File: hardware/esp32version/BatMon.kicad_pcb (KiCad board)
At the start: 2 copper layers, 47 x 24.1 mm, 30 parts, among them J1 Battery Connector, J2 Battery_Passthrough, J3 Conn_01x06_Pin, J4 RESET, Q1 Q_PMOS_DDGSDD_TSOP-6, Q2 Q_PMOS_DDGSDD_TSOP-6, Q3 SS8050-G, U1 ESP32-WROOM-32D, U2 LM2904, U3 AMS1117

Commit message: updated PCB
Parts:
- added R10: 22k, Resistor_SMD:R_0603_1608Metric_Pad0.98x0.95mm_HandSolder, F.Cu at (161.6, 54.6)
- added R3: 5k, Resistor_SMD:R_0603_1608Metric_Pad0.98x0.95mm_HandSolder, F.Cu at (161.6, 49.6)
- added R9: 22k, Resistor_SMD:R_0603_1608Metric_Pad0.98x0.95mm_HandSolder, F.Cu at (161.6, 52.1)
- D1, D2: value D_Zener -> D_Zener_ANK
- J1: value Battery Connector -> Battery_Connector
- J2: value Battery_Passthrough -> Charging_Connector
- J3: value Conn_01x06_Pin -> Prog_Connector
- R11: value k -> 22k
- U2: footprint Package_DIP:DIP-8_W8.89mm_SMDSocket_LongPads -> Package_SO:SOIC-8_3.9x4.9mm_P1.27mm
- moved D1 35.4 mm to (156.0, 50.6)
- moved D2 33.0 mm to (155.4, 58.1)
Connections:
- net Cell2 renamed C2ADC
- net Net-(J1-Pin_2) renamed /C1RAW
- net Net-(J1-Pin_3) renamed /C2RAW
- C1 pad 2: GND -> CGND
- C2 pad 1: +BATT -> C2IN
- C2 pad 2: GND -> CGND
- C3 pad 2: GND -> CGND
- C4 pad 2: GND -> CGND
- C5 pad 2: GND -> CGND
- D1 pad 1: +BATT -> Net-(Q1-G)
- D1 pad 2: Net-(D1-A) -> unconnected-(D1-A-Pad2)
- D1 pad 3: (no net) -> C2IN
- D2 pad 1: C1IN -> Net-(Q2-G)
- D2 pad 2: Net-(D2-A) -> unconnected-(D2-A-Pad2)
- D2 pad 3: (no net) -> C1IN
- J1 pad 1: GND -> CGND
- J2 pad 5: GND -> CGND
- J3 pad 5: GND -> CGND
- J4 pad 1: GND -> CGND
- Q1 pad 3: Net-(D1-A) -> Net-(Q1-G)
- Q1 pad 4: +BATT -> C2IN
- Q2 pad 3: Net-(D2-A) -> Net-(Q2-G)
- Q3 pad 2: GND -> CGND
- R11 pad 2: +BATT -> C2IN
- R12 pad 1: GND -> CGND
- R4 pad 1: GND -> Net-(U2A--)
- R4 pad 2: Net-(U2A--) -> CGND
- R6 pad 2: GND -> CGND
- R7 pad 2: Net-(D1-A) -> Net-(Q1-G)
- R8 pad 1: GND -> CGND
- R8 pad 2: Net-(D2-A) -> Net-(Q2-G)
- U1 pad 1: GND -> CGND
- U1 pad 15: GND -> CGND
- U1 pad 27: Cell1 -> C1ADC
- U1 pad 38: GND -> CGND
- U1 pad 39: GND -> CGND
- U2 pad 4: GND -> CGND
- U3 pad 1: GND -> CGND
- U3 pad 3: +BATT -> C2IN
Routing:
- net C2IN: track 0.00 -> 28.0 mm, vias 0 -> 2
- net +BATT: track 28.0 -> 0.00 mm, vias 2 -> 0
- net GND: track 81.4 -> 64.1 mm, vias 5 -> 0
- net CGND: track 0.00 -> 17.3 mm, vias 0 -> 5
- net Net-(Q1-G): track 0.00 -> 12.7 mm
- net Net-(D1-A): track 12.7 -> 0.00 mm
- net Net-(Q2-G): track 0.00 -> 11.7 mm
- net Net-(D2-A): track 11.7 -> 0.00 mm
- added copper zone on B.Cu, net CGND
- added copper zone on F.Cu, net CGND
- removed copper zone on B.Cu, net GND
- removed copper zone on F.Cu, net GND

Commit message: started working on new layout
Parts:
- removed J2: Charging_Connector, Connector_PinHeader_2.54mm:PinHeader_1x05_P2.54mm_Horizontal
- removed J4: RESET, Connector_PinHeader_2.54mm:PinHeader_1x02_P2.54mm_Vertical
- removed the R10 at (135.7, 81.3)
- removed the R10 at (161.6, 54.6)
- removed the R3 at (161.6, 49.6)
- removed the R3 at (115.8, 80.2)
- removed the R9 at (118.3, 79.2)
- removed the R9 at (161.6, 52.1)
- removed U3: AMS1117, Package_TO_SOT_SMD:SOT-223-3_TabPin2
- added D3: D_Schottky, Diode_SMD:D_SOD-123, F.Cu at (101.2, 68.6)
- added D4: LED, LED_SMD:LED_0603_1608Metric_Pad1.05x0.95mm_HandSolder, F.Cu at (108.0, 67.3)
- added D5: ~, ELEKTRON_Footprints:D_TVS_Quad_Array_1206, B.Cu at (142.6, 81.3)
- added J5: Charging_Connector, ELEKTRON_Footprints:Conn_Edge_1x6_LLSSSS_Mirrored, F.Cu at (149.0, 79.0)
- added R10: 22k, Resistor_SMD:R_0603_1608Metric_Pad0.98x0.95mm_HandSolder, F.Cu at (162.6, 63.5)
- added R3: R, Resistor_SMD:R_0603_1608Metric_Pad0.98x0.95mm_HandSolder, F.Cu at (114.7, 68.6)
- added R9: 20k, Resistor_SMD:R_0603_1608Metric_Pad0.98x0.95mm_HandSolder, F.Cu at (228.8, 110.5)
- added U4: AZ1117CR-3.3, Package_TO_SOT_SMD:SOT-89-3_Handsoldering, F.Cu at (196.0, 64.8)
- BZ1, U1: moved to F.Cu
- C1: footprint Capacitor_SMD:C_0603_1608Metric_Pad1.08x0.95mm_HandSolder -> Capacitor_Tantalum_SMD:CP_EIA-3216-18_Kemet-A_Pad1.58x1.35mm_HandSolder
- C2: value 100n -> 22µ; footprint Capacitor_SMD:C_0603_1608Metric_Pad1.08x0.95mm_HandSolder -> Capacitor_Tantalum_SMD:CP_EIA-3216-18_Kemet-A_Pad1.58x1.35mm_HandSolder
- J1: footprint Connector_PinHeader_2.54mm:PinHeader_1x03_P2.54mm_Horizontal -> Connector_JST:JST_XH_S3B-XH-A_1x03_P2.50mm_Horizontal
- J3: footprint Connector_PinHeader_2.54mm:PinHeader_1x06_P2.54mm_Vertical -> ELEKTRON_Footprints:Dbg_Port_1x6_P1.27mm_ThroughHole
- R1: value 5k -> 30k
- R11: value 22k -> 30k
- R2, R4: value 5k -> 10k
- moved R6 122.5 mm to (224.5, 115.5), turned to 0 degrees
- moved R5 120.1 mm to (224.5, 113.0), turned to 0 degrees
- moved R4 114.3 mm to (224.5, 110.5), turned to 0 degrees
- moved R8 106.5 mm to (228.8, 108.0), turned to 0 degrees
- moved C4 102.4 mm to (204.5, 74.9)
- moved R11 101.6 mm to (214.6, 61.0), turned to 0 degrees
- moved R2 101.4 mm to (207.4, 61.0)
- moved R12 96.6 mm to (209.2, 58.4), turned to 0 degrees
- moved R1 92.7 mm to (203.2, 57.1), turned to 0 degrees
- moved U2 91.6 mm to (195.9, 58.6), turned to 0 degrees
- moved C5 87.1 mm to (204.5, 78.7), turned to 0 degrees
- moved C1 86.0 mm to (197.0, 48.2), turned to 0 degrees
- moved C2 82.1 mm to (197.0, 51.4), turned to 0 degrees
- moved D1 69.0 mm to (97.8, 87.6)
- moved BZ1 66.3 mm to (191.3, 85.9), turned to 0 degrees
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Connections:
- net /C1RAW renamed Net-(D5D-A1)
- net /C2RAW renamed Net-(D5C-A1)
- C1 pad 2: CGND -> GND
- C2 pad 2: CGND -> GND
- C3 pad 2: CGND -> GND
- C4 pad 2: CGND -> GND
- C5 pad 2: CGND -> GND
- J1 pad 1: CGND -> GND
- J3 pad 5: CGND -> GND
- Q3 pad 2: CGND -> GND
- R1 pad 1: Net-(U2B--) -> Net-(U2B-+)
- R1 pad 2: Net-(U2A-+) -> C2IN
- R11 pad 1: Net-(U2B-+) -> Net-(U2B--)
- R11 pad 2: C2IN -> C1IN
- R12 pad 1: CGND -> C2ADC
- R12 pad 2: Net-(U2B-+) -> Net-(U2B--)
- R2 pad 1: Net-(U2A-+) -> Net-(U2B-+)
- R2 pad 2: C2ADC -> GND
- R4 pad 1: Net-(U2A--) -> C1ADC
- R4 pad 2: CGND -> GND
- R6 pad 2: CGND -> GND
- R8 pad 1: CGND -> GND
- U1 pad 1: CGND -> GND
- U1 pad 11: unconnected-(U1-IO26-Pad11) -> Net-(U1-IO26)
- U1 pad 15: CGND -> GND
- U1 pad 38: CGND -> GND
- U1 pad 39: CGND -> GND
- U2 pad 1: C2ADC -> unconnected-(U2-Pad1)
- U2 pad 2: Net-(U2A--) -> unconnected-(U2A---Pad2)
- U2 pad 3: Net-(U2A-+) -> unconnected-(U2A-+-Pad3)
- U2 pad 4: CGND -> GND
- U2 pad 7: Net-(U2B--) -> C2ADC
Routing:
- net +3.3V: track 90.4 -> 4.05 mm, vias 2 -> 1
- net Net-(J3-Pin_1): track 80.0 -> 0.00 mm, vias 1 -> 0
- net GND: track 64.1 -> 6.83 mm, vias 0 -> 3
- net SDA: track 36.4 -> 0.00 mm, vias 2 -> 0
- net SCL: track 36.8 -> 2.76 mm, vias 2 -> 0
- net Net-(D5D-A1): track 31.3 -> 0.00 mm
- net Net-(J3-Pin_4): track 30.3 -> 0.00 mm
- net C2IN: track 28.0 -> 0.00 mm, vias 2 -> 0
- net Net-(J3-Pin_3): track 25.1 -> 0.00 mm
- net Net-(D5C-A1): track 22.5 -> 2.96 mm, vias 1 -> 0
- net C1IN: track 18.9 -> 0.00 mm, vias 2 -> 0
- net CGND: track 17.3 -> 0.00 mm, vias 5 -> 0
- net Net-(U2A--): track 15.5 -> 0.00 mm, vias 2 -> 0
- net Net-(BZ1-+): track 13.9 -> 0.00 mm, vias 1 -> 0
- net C2ADC: track 13.6 -> 0.00 mm, vias 1 -> 0
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- added copper zone on In1.Cu, net +3.3V
- added copper zone on In2.Cu, net GND
- removed copper zone on B.Cu, net CGND
- removed copper zone on F.Cu, net CGND
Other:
- board size 47 x 24.1 mm -> 24 x 35 mm
- copper layers 2 -> 4
- board text removed: "BatMon V0.1"
- board text removed: "EN"
- board text removed: "GND"
- board text removed: "IO0"
- board text removed: "RESET"
- board text removed: "RX"
- board text removed: "S1"
- board text removed: "S2"
- board text removed: "SCL"
- board text removed: "SDA"
- board text removed: "TX"
- board text removed: "VDD"

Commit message: first iteration of new pcb done
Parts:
- BZ1, C4, C5, D3, Q3, R1, R11, R12, R2, R4, R5, R9, U2: moved to B.Cu
- D1, D2: footprint Package_TO_SOT_SMD:TSOT-23_HandSoldering -> Package_TO_SOT_SMD:TSOT-23
- R10: value 22k -> 10k; moved to B.Cu
- R6: value 22k -> 10k
- moved R9 111.4 mm to (125.1, 69.8), turned to 90 degrees
- moved R8 111.3 mm to (121.3, 79.4), turned to 90 degrees
- moved R6 110.9 mm to (121.3, 74.9), turned to -90 degrees
- moved R4 108.9 mm to (125.1, 66.0), turned to 90 degrees
- moved R5 93.5 mm to (136.5, 81.3), turned to 90 degrees
- moved R11 83.4 mm to (131.8, 70.5), turned to 180 degrees
- moved R12 75.4 mm to (134.6, 69.5), turned to -90 degrees
- moved C4 72.9 mm to (131.9, 68.6), turned to 180 degrees
- moved C2 69.9 mm to (132.7, 78.7), turned to 90 degrees
- moved R2 69.5 mm to (138.4, 69.5), turned to -90 degrees
- moved R1 67.8 mm to (136.5, 69.5), turned to -90 degrees
- moved C5 66.1 mm to (138.4, 81.3), turned to -90 degrees
- moved BZ1 65.7 mm to (126.1, 77.8), turned to 180 degrees
- moved C1 62.7 mm to (142.2, 78.7), turned to 90 degrees
- moved U2 60.8 mm to (135.3, 63.5), turned to -90 degrees
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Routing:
- net Net-(D5D-A1): track 0.00 -> 42.1 mm
- net GND: track 6.83 -> 45.2 mm, vias 3 -> 10
- net +3.3V: track 4.05 -> 32.7 mm, vias 1 -> 4
- net Net-(D5C-A1): track 2.96 -> 31.4 mm
- net SDA: track 0.00 -> 26.0 mm, vias 0 -> 1
- net SCL: track 2.76 -> 28.7 mm, vias 0 -> 2
- net C2IN: track 0.00 -> 25.2 mm, vias 0 -> 1
- net Net-(J3-Pin_1): track 0.00 -> 22.1 mm, vias 0 -> 1
- net C1IN: track 0.00 -> 20.2 mm, vias 0 -> 1
- net C1ADC: track 0.00 -> 19.0 mm, vias 0 -> 1
- net Net-(J3-Pin_2): track 0.00 -> 17.1 mm, vias 0 -> 1
- net C2ADC: track 0.00 -> 14.7 mm, vias 0 -> 1
- net Net-(BZ1-+): track 0.00 -> 10.3 mm
- net Net-(Q2-G): track 0.00 -> 9.59 mm
- net Buzzer: track 0.00 -> 9.23 mm, vias 0 -> 1
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
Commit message: minor changes, round corners
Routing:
- net GND: track 45.2 -> 44.2 mm
- net Net-(J3-Pin_2): track 17.1 -> 17.6 mm
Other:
- outline, holes or cut-outs redrawn

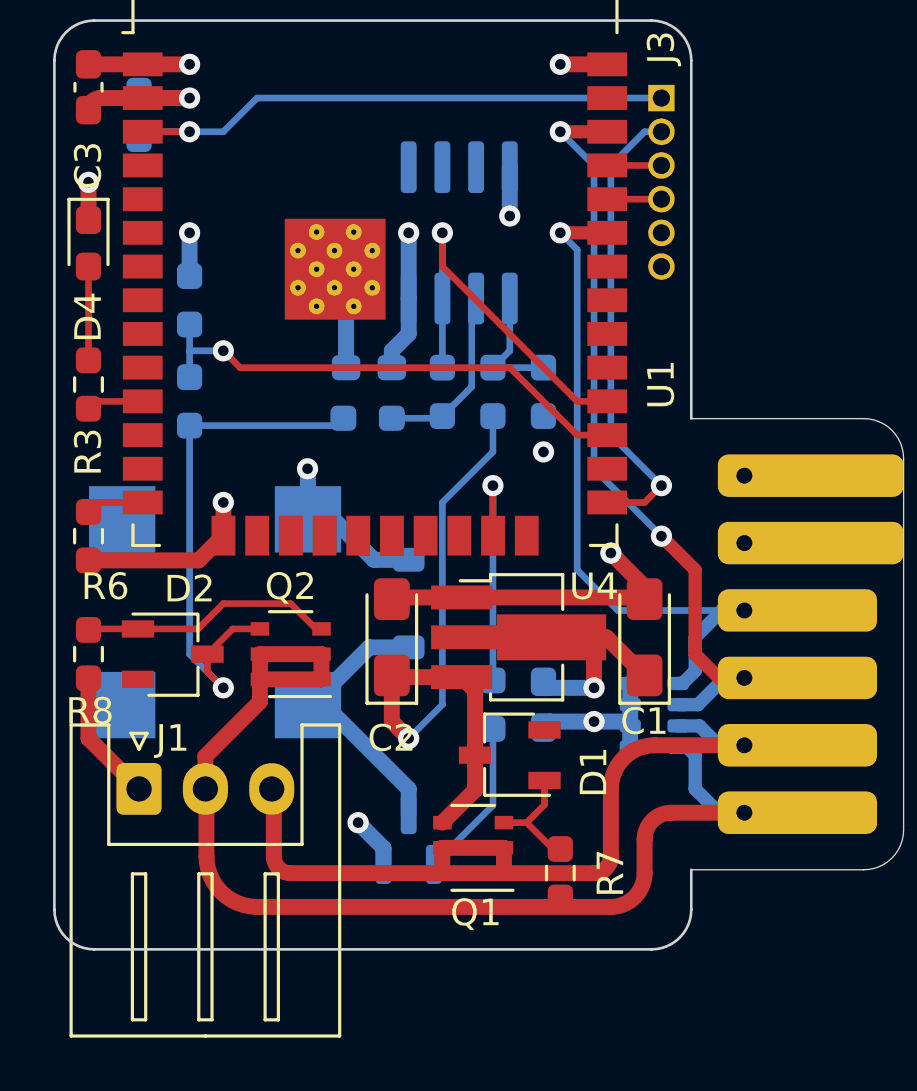
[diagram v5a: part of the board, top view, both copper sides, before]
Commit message: added a switch and fixed the battery pinout
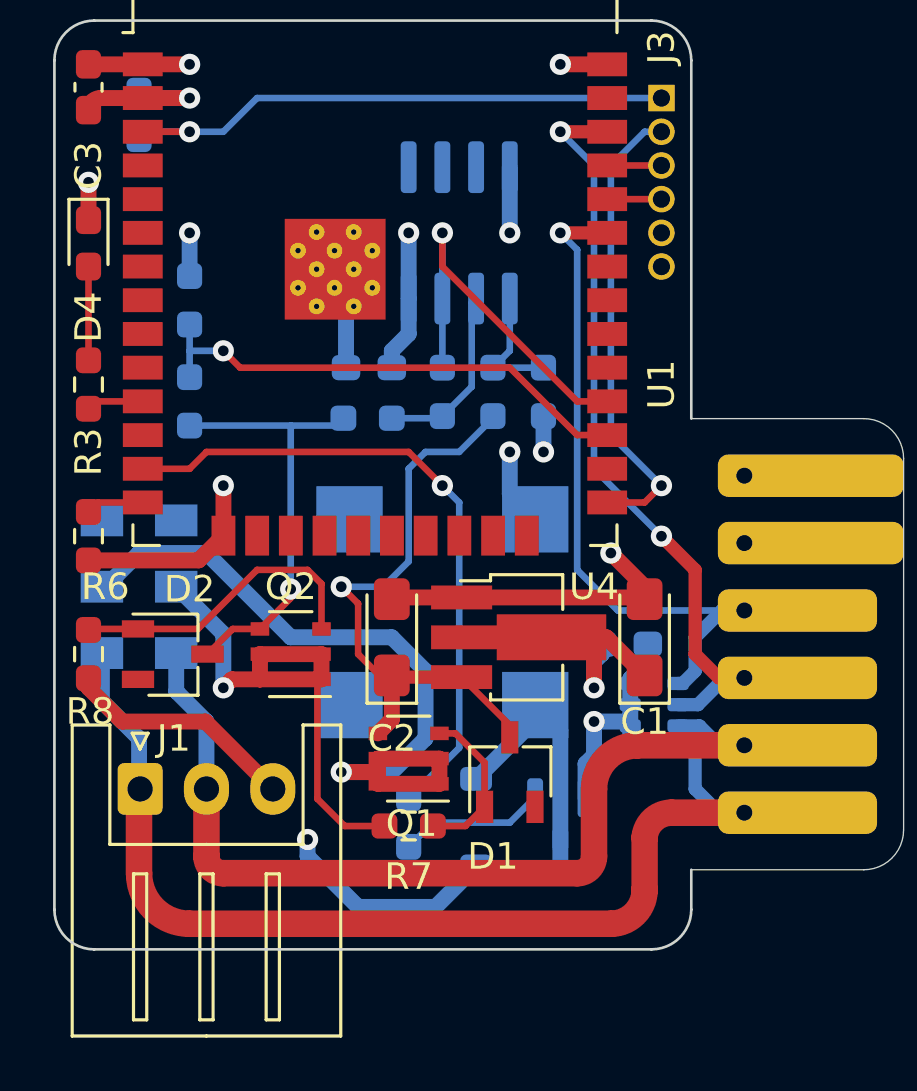
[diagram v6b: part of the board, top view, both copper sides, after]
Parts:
- added SW1: POWER_SW, ELEKTRON_Footprints:SW_DPDT_Nidec_CL-SB-22A-1x, B.Cu at (123.2, 76.8)
- moved D3 8.64 mm to (135.9, 85.7), turned to 90 degrees
- moved BZ1 8.56 mm to (134.6, 77.8)
- moved R7 5.99 mm to (133.3, 85.9), turned to 0 degrees
- moved Q3 5.75 mm to (139.1, 85.7), turned to -90 degrees
- moved R5 5.46 mm to (133.3, 85.7)
- moved Q1 4.15 mm to (133.3, 83.3)
- moved C5 3.82 mm to (141.5, 79.0), turned to 0 degrees
- moved D1 0.63 mm to (137.2, 83.8), turned to 90 degrees
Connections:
- D5 pad 3: Net-(D5C-A1) -> /C1RAW
- D5 pad 4: Net-(D5D-A1) -> /C2RAW
- J1 pad 1: GND -> /C2RAW
- J1 pad 2: Net-(D5D-A1) -> /C1RAW
- J1 pad 3: Net-(D5C-A1) -> GND
- J5 pad 5: Net-(D5C-A1) -> /C1RAW
- J5 pad 6: Net-(D5D-A1) -> /C2RAW
- Q1 pad 1: Net-(D5C-A1) -> Net-(SW1B-B)
- Q1 pad 2: Net-(D5C-A1) -> Net-(SW1B-B)
- Q1 pad 5: Net-(D5C-A1) -> Net-(SW1B-B)
- Q1 pad 6: Net-(D5C-A1) -> Net-(SW1B-B)
- Q2 pad 1: Net-(D5D-A1) -> Net-(SW1A-B)
- Q2 pad 2: Net-(D5D-A1) -> Net-(SW1A-B)
- Q2 pad 5: Net-(D5D-A1) -> Net-(SW1A-B)
- Q2 pad 6: Net-(D5D-A1) -> Net-(SW1A-B)
- R7 pad 1: Net-(D5D-A1) -> Net-(SW1A-B)
- U1 pad 13: unconnected-(U1-IO14-Pad13) -> Buzzer
- U1 pad 23: Buzzer -> unconnected-(U1-IO15-Pad23)
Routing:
- net Net-(D5D-A1): track 42.1 -> 0.00 mm
- net /C2RAW: track 0.00 -> 40.1 mm
- net /C1RAW: track 0.00 -> 35.3 mm
- net Net-(D5C-A1): track 31.4 -> 0.00 mm
- net Net-(SW1B-B): track 0.00 -> 28.7 mm, vias 0 -> 1
- net Net-(SW1A-B): track 0.00 -> 20.2 mm, vias 0 -> 1
- net Buzzer: track 9.23 -> 24.9 mm
- net GND: track 44.2 -> 51.6 mm, vias 10 -> 9
- net +3.3V: track 32.7 -> 38.4 mm, vias 4 -> 5
- net C1IN: track 20.2 -> 16.4 mm
- net Net-(Q2-G): track 9.59 -> 11.6 mm
- net C2IN: track 25.2 -> 23.2 mm
- net Net-(Q1-G): track 4.41 -> 6.07 mm
- net Net-(BZ1-+): track 10.3 -> 9.46 mm

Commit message: finalized design and exported gerbers
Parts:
- added C6: 22µ, Capacitor_Tantalum_SMD:CP_EIA-3216-18_Kemet-A_Pad1.58x1.35mm_HandSolder, B.Cu at (123.2, 63.5)
- added Q4: SS8050-G, Package_TO_SOT_SMD:SOT-23, B.Cu at (127.6, 57.8)
- added Q5: SS8050-G, Package_TO_SOT_SMD:SOT-23, B.Cu at (127.6, 61.3)
- added R13: 10k, Resistor_SMD:R_0603_1608Metric_Pad0.98x0.95mm_HandSolder, B.Cu at (135.3, 57.8)
- added R14: 10k, Resistor_SMD:R_0603_1608Metric_Pad0.98x0.95mm_HandSolder, B.Cu at (130.8, 59.4)
- moved U2 0.63 mm to (135.9, 63.5)
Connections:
- net Net-(J3-Pin_3) renamed /TXD
- net Net-(J3-Pin_4) renamed /RXD
- J3 pad 1: Net-(J3-Pin_1) -> PROG_RTS
- J3 pad 2: Net-(J3-Pin_2) -> PROG_DTR
- R10 pad 1: Net-(J3-Pin_1) -> ESP_EN
- U1 pad 25: Net-(J3-Pin_2) -> ESP_IO0
- U1 pad 3: Net-(J3-Pin_1) -> ESP_EN
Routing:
- net ESP_IO0: track 0.00 -> 23.4 mm, vias 0 -> 1
- net Net-(J3-Pin_1): track 22.1 -> 0.00 mm, vias 1 -> 0
- net Net-(J3-Pin_2): track 17.6 -> 0.00 mm, vias 1 -> 0
- net PROG_DTR: track 0.00 -> 16.9 mm
- net PROG_RTS: track 0.00 -> 14.9 mm
- net ESP_EN: track 0.00 -> 8.82 mm, vias 0 -> 1
- net Net-(Q4-B): track 0.00 -> 6.70 mm
- net Net-(Q5-B): track 0.00 -> 2.35 mm
- net GND: track 51.6 -> 53.8 mm
- added copper zone on B.Cu, net GND
- added copper zone on F.Cu, net GND
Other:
- board text added: "+"
- board text added: "-"
- board text added: "1"
- board text added: "2"
- board text added: "BatMon ©fb 2023 23009"
- board text added: "C"
- board text added: "C1"
- board text added: "C2"
- board text added: "D"
- board text added: "Debug"
- board text added: "GND"
- board text added: "JLCJLCJLCJLC"
- board text added: "OFF"
- board text added: "ON"
- board text added: "RTS DTR TXD RXD GND 3v3"

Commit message: added part fields and bom
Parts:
- R3: value R -> 330
